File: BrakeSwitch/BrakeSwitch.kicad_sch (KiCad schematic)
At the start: 9 parts, among them J1 12V_in, J2 LightPlug, J3 5V_out, J4 Sensor_in, Q1 NMOS, U2 LMV321

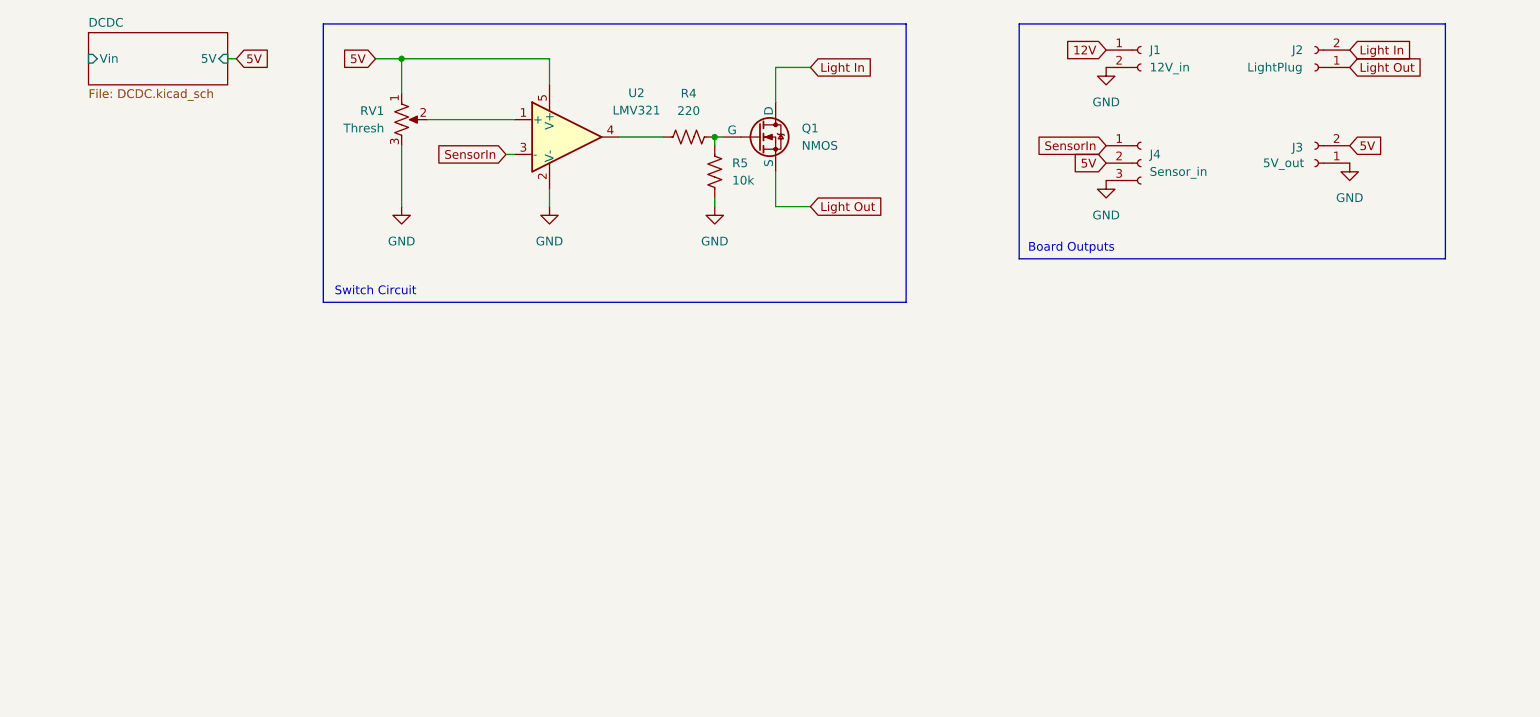
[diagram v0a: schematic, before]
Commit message: Assigned most footprints
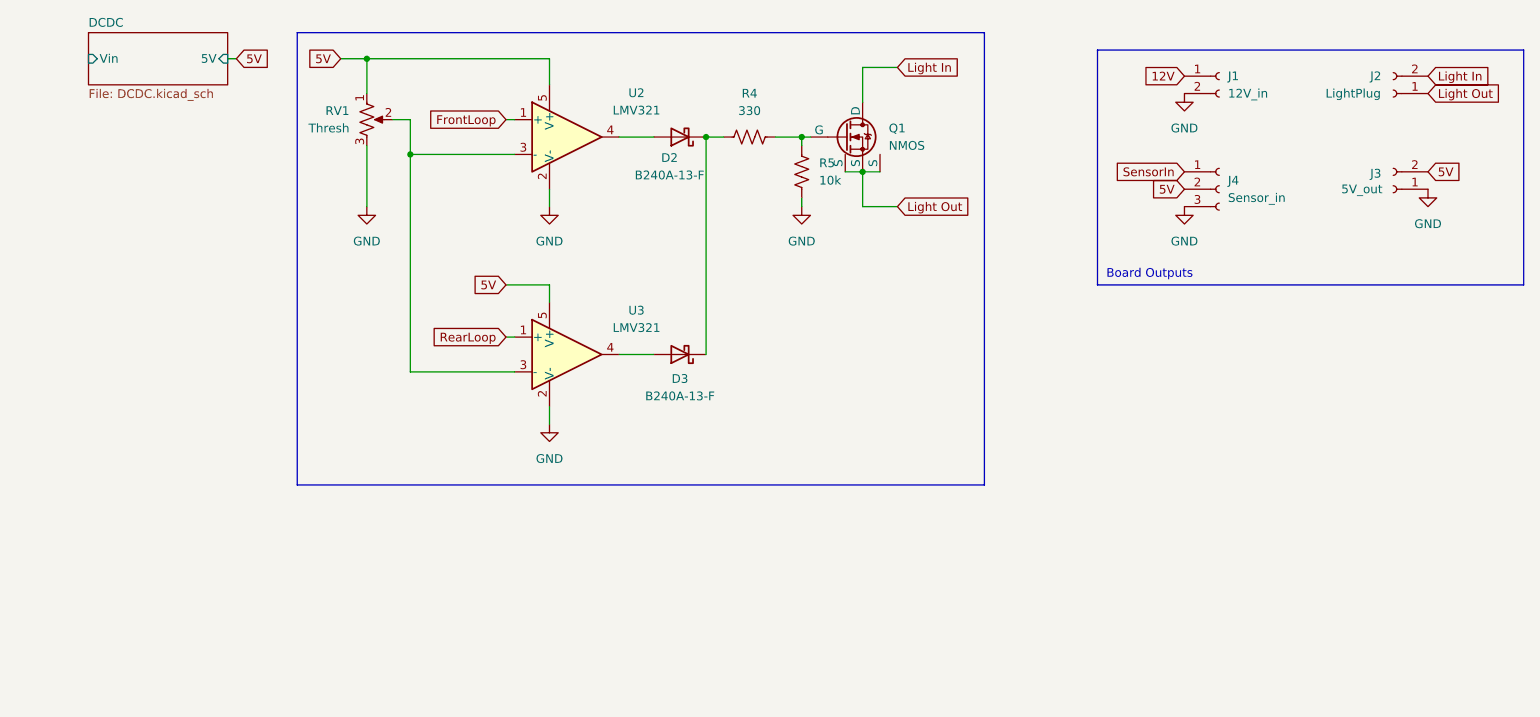
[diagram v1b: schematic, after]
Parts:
- added D2, D3: B240A-13-F, Diode_SMD:D_SMA, symbol Device:D_Schottky
- added U3: LMV321, Package_TO_SOT_SMD:SOT-23-5, symbol Amplifier_Operational:LMV321
- Q1: footprint (none) -> Package_SO:Vishay_PowerPAK_1212-8_Single; DigiKey (none) -> https://www.digikey.com/en/products/detail/onsemi/NTTFS5C45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
- R4: value 220 -> 330; footprint (none) -> Resistor_SMD:R_0603_1608Metric
- R5: footprint (none) -> Resistor_SMD:R_0603_1608Metric
- RV1: footprint (none) -> Potentiometer_THT:Potentiometer_Runtron_RM-065_Vertical; DigiKey (none) -> https://www.digikey.com/en/products/detail/amphenol-piher-s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
- U2: footprint (none) -> Package_TO_SOT_SMD:SOT-23-5; DigiKey (none) -> https://www.digikey.com/en/products/detail/texas-instrument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
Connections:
- net 5V: now also U3.5 (V+)
- net GND: now also U3.2 (V-)
- net Light In: now also Q1.5 (D); no longer Q1.1 (D)
- net Light Out: now also Q1.1 (S), Q1.2 (S)
- net SensorIn: no longer U2.3 (-)
- net at R4.1: now also D2.1 (K), D3.1 (K); no longer U2.4
- net at R4.2, R5.1: now also Q1.4 (G); no longer Q1.2 (G)
- net at RV1.2: now also U2.3 (-), U3.3 (-); no longer U2.1 (+)
- new net: D3.2 (A), U3.4
- new net: D2.2 (A), U2.4
- new net FrontLoop: U2.1 (+)
- new net RearLoop: U3.1 (+)
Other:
- note removed: "Switch Circuit"
- moved on the sheet: J1, J2, J3, J4, R4, R5, RV1

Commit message: betime
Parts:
- added J5: Back_Pads, symbol Connector:Conn_01x03_Socket
- J4: value Sensor_in -> Front_Pads
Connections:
- net SensorIn is gone; now on net FrontLoop: J4.1 (Pin_1)
- net 5V: now also J5.2 (Pin_2)
- net GND: now also J5.3 (Pin_3)
- new net BackLoop: J5.1 (Pin_1)
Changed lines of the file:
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@@
 	(rectangle
 		(start 171.45 22.86)
-		(end 233.68 57.15)
+		(end 233.68 76.2)
 		(stroke
 			(width 0)
@@
 	(text "Board Outputs"
 		(exclude_from_sim no)
-		(at 179.07 55.626 0)
+		(at 178.562 74.676 0)
 		(effects
 			(font
@@
 		)
 	)
+	(global_label "BackLoop"
+		(shape input)
+		(at 184.15 55.88 180)
+		(fields_autoplaced yes)
+		(effects
+			(font
+				(size 1.27 1.27)
+			)
+			(justify right)
+		)
+		(property "Intersheetrefs" "${INTERSHEET_REFS}"
+			(at 172.154 55.88 0)
+			(effects
+				(font
+					(size 1.27 1.27)
+				)
+				(justify right)
+				(hide yes)
+			)
+		)
+	)
 	(global_label "FrontLoop"
 		(shape input)
@@
 		)
 	)
+	(global_label "FrontLoop"
+		(shape input)
+		(at 184.15 40.64 180)
+		(fields_autoplaced yes)
+		(effects
+			(font
+				(size 1.27 1.27)
+			)
+			(justify right)
+		)
+		(property "Intersheetrefs" "${INTERSHEET_REFS}"
+			(at 171.7912 40.64 0)
+			(effects
+				(font
+					(size 1.27 1.27)
+				)
+				(justify right)
+				(hide yes)
+			)
+		)
+	)
 	(global_label "Light In"
 		(shape input)
@@
 		)
 	)
-	(global_label "SensorIn"
+	(global_label "5V"
 		(shape input)
-		(at 184.15 40.64 180)
+		(at 184.15 58.42 180)
 		(fields_autoplaced yes)
 		(effects
@@
 		)
 		(property "Intersheetrefs" "${INTERSHEET_REFS}"
-			(at 173.0006 40.64 0)
+			(at 178.8667 58.42 0)
 			(effects
 				(font
@@
 	)
 	(symbol
+		(lib_id "Connector:Conn_01x03_Socket")
+		(at 189.23 58.42 0)
+		(unit 1)
+		(exclude_from_sim no)
+		(in_bom yes)
+		(on_board yes)
+		(dnp no)
+		(fields_autoplaced yes)
+		(property "Reference" "J5"
+			(at 190.5 57.1499 0)
+			(effects
+				(font
+					(size 1.27 1.27)
+				)
+				(justify left)
+			)
+		)
+		(property "Value" "Back_Pads"
+			(at 190.5 59.6899 0)
+			(effects
+				(font
+					(size 1.27 1.27)
+				)
+				(justify left)
+			)
+		)
+		(property "Footprint" ""
+			(at 189.23 58.42 0)
+			(effects
+				(font
+					(size 1.27 1.27)
+				)
+				(hide yes)
+			)
+		)
+		(property "Datasheet" "~"
+			(at 189.23 58.42 0)
+			(effects
+				(font
+					(size 1.27 1.27)
+				)
+				(hide yes)
+			)
+		)
+		(property "Description" "Generic connector, single row, 01x03, script generated"
+			(at 189.23 58.42 0)
+			(effects
+				(font
+					(size 1.27 1.27)
+				)
+				(hide yes)
+			)
+		)
+		(pin "2"
+		)
+		(pin "1"
+		)
+		(pin "3"
+		)
+		(instances
+			(project "BrakeSwitch"
+				(path "/fe3f2fb8-8742-4f31-813f-1dad9d418d71"
+					(reference "J5")
+					(unit 1)
+				)
+			)
+		)
+	)
+	(symbol
 		(lib_id "Connector:Conn_01x02_Socket")
 		(at 214.63 43.18 180)
@@
 	)
 	(symbol
+		(lib_id "power:GND")
+		(at 184.15 60.96 0)
+		(unit 1)
+		(exclude_from_sim no)
+		(in_bom yes)
+		(on_board yes)
+		(dnp no)
+		(fields_autoplaced yes)
+		(property "Reference" "#PWR013"
+			(at 184.15 67.31 0)
+			(effects
+				(font
+					(size 1.27 1.27)
+				)
+				(hide yes)
+			)
+		)
+		(property "Value" "GND"
+			(at 184.15 66.04 0)
+			(effects
+				(font
+					(size 1.27 1.27)
+				)
+			)
+		)
+		(property "Footprint" ""
+			(at 184.15 60.96 0)
+			(effects
+				(font
+					(size 1.27 1.27)
+				)
+				(hide yes)
+			)
+		)
+		(property "Datasheet" ""
+			(at 184.15 60.96 0)
+			(effects
+				(font
+					(size 1.27 1.27)
+				)
+				(hide yes)
+			)
+		)
+		(property "Description" "Power symbol creates a global label with name \"GND\" , ground"
+			(at 184.15 60.96 0)
+			(effects
+				(font
+					(size 1.27 1.27)
+				)
+				(hide yes)
+			)
+		)
+		(pin "1"
+		)
+		(instances
+			(project "BrakeSwitch"
+				(path "/fe3f2fb8-8742-4f31-813f-1dad9d418d71"
+					(reference "#PWR013")
+					(unit 1)
+				)
+			)
+		)
+	)
+	(symbol
 		(lib_id "Connector:Conn_01x03_Socket")
 		(at 189.23 43.18 0)
@@
 			)
 		)
-		(property "Value" "Sensor_in"
+		(property "Value" "Front_Pads"
 			(at 190.5 44.4499 0)
 			(effects

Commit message: Basic layout done
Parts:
- added J6: 12V_in, AA-Custom:SolderPad_01x02, symbol Connector:Conn_01x02_Socket
- J1, J2, J3: footprint (none) -> AA-Custom:SolderPad_01x02
- J4, J5: footprint (none) -> AA-Custom:SolderPad_01x03
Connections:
- net BackLoop is gone; now on net RearLoop: J5.1 (Pin_1)
- net GND: now also J6.2 (Pin_2)
- new net 12V_out: J6.1 (Pin_1)
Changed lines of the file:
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@@
 		)
 	)
-	(global_label "BackLoop"
+	(global_label "RearLoop"
 		(shape input)
 		(at 184.15 55.88 180)
@@
 		)
 		(property "Intersheetrefs" "${INTERSHEET_REFS}"
-			(at 172.154 55.88 0)
+			(at 172.3959 55.88 0)
 			(effects
 				(font
@@
 		)
 	)
+	(global_label "12V_out"
+		(shape input)
+		(at 219.71 55.88 0)
+		(fields_autoplaced yes)
+		(effects
+			(font
+				(size 1.27 1.27)
+			)
+			(justify left)
+		)
+		(property "Intersheetrefs" "${INTERSHEET_REFS}"
+			(at 230.1941 55.88 0)
+			(effects
+				(font
+					(size 1.27 1.27)
+				)
+				(justify left)
+				(hide yes)
+			)
+		)
+	)
 	(global_label "5V"
 		(shape input)
@@
 	)
 	(symbol
+		(lib_id "Connector:Conn_01x02_Socket")
+		(at 214.63 55.88 0)
+		(mirror y)
+		(unit 1)
+		(exclude_from_sim no)
+		(in_bom yes)
+		(on_board yes)
+		(dnp no)
+		(fields_autoplaced yes)
+		(property "Reference" "J6"
+			(at 213.36 55.8799 0)
+			(effects
+				(font
+					(size 1.27 1.27)
+				)
+				(justify left)
+			)
+		)
+		(property "Value" "12V_in"
+			(at 213.36 58.4199 0)
+			(effects
+				(font
+					(size 1.27 1.27)
+				)
+				(justify left)
+			)
+		)
+		(property "Footprint" "AA-Custom:SolderPad_01x02"
+			(at 214.63 55.88 0)
+			(effects
+				(font
+					(size 1.27 1.27)
+				)
+				(hide yes)
+			)
+		)
+		(property "Datasheet" "~"
+			(at 214.63 55.88 0)
+			(effects
+				(font
+					(size 1.27 1.27)
+				)
+				(hide yes)
+			)
+		)
+		(property "Description" "Generic connector, single row, 01x02, script generated"
+			(at 214.63 55.88 0)
+			(effects
+				(font
+					(size 1.27 1.27)
+				)
+				(hide yes)
+			)
+		)
+		(pin "2"
+		)
+		(pin "1"
+		)
+		(instances
+			(project "BrakeSwitch"
+				(path "/fe3f2fb8-8742-4f31-813f-1dad9d418d71"
+					(reference "J6")
+					(unit 1)
+				)
+			)
+		)
+	)
+	(symbol
 		(lib_id "Device:R_US")
 		(at 120.65 35.56 90)
@@
 	(symbol
 		(lib_id "power:GND")
+		(at 219.71 58.42 0)
+		(mirror y)
+		(unit 1)
+		(exclude_from_sim no)
+		(in_bom yes)
+		(on_board yes)
+		(dnp no)
+		(fields_autoplaced yes)
+		(property "Reference" "#PWR016"
+			(at 219.71 64.77 0)
+			(effects
+				(font
+					(size 1.27 1.27)
+				)
+				(hide yes)
+			)
+		)
+		(property "Value" "GND"
+			(at 219.71 63.5 0)
+			(effects
+				(font
+					(size 1.27 1.27)
+				)
+			)
+		)
+		(property "Footprint" ""
+			(at 219.71 58.42 0)
+			(effects
+				(font
+					(size 1.27 1.27)
+				)
+				(hide yes)
+			)
+		)
+		(property "Datasheet" ""
+			(at 219.71 58.42 0)
+			(effects
+				(font
+					(size 1.27 1.27)
+				)
+				(hide yes)
+			)
+		)
+		(property "Description" "Power symbol creates a global label with name \"GND\" , ground"
+			(at 219.71 58.42 0)
+			(effects
+				(font
+					(size 1.27 1.27)
+				)
+				(hide yes)
+			)
+		)
+		(pin "1"
+		)
+		(instances
+			(project "BrakeSwitch"
+				(path "/fe3f2fb8-8742-4f31-813f-1dad9d418d71"
+					(reference "#PWR016")
+					(unit 1)
+				)
+			)
+		)
+	)
+	(symbol
+		(lib_id "power:GND")
 		(at 64.77 45.72 0)
 		(unit 1)
@@
 			)
 		)
-		(property "Footprint" ""
+		(property "Footprint" "AA-Custom:SolderPad_01x02"
 			(at 189.23 26.67 0)
 			(effects
@@
 			)
 		)
-		(property "Footprint" ""
+		(property "Footprint" "AA-Custom:SolderPad_01x02"
 			(at 214.63 29.21 0)
 			(effects
@@
 			)
 		)
-		(property "Footprint" ""
+		(property "Footprint" "AA-Custom:SolderPad_01x03"
 			(at 189.23 58.42 0)
 			(effects
@@
 			)
 		)
-		(property "Footprint" ""
+		(property "Footprint" "AA-Custom:SolderPad_01x02"
 			(at 214.63 43.18 0)
 			(effects
@@
 			)
 		)
-		(property "Footprint" ""
+		(property "Footprint" "AA-Custom:SolderPad_01x03"
 			(at 189.23 43.18 0)
 			(effects
@@
 					(reference "Q1")
 					(unit 1)
+				)
+				(path "/fe3f2fb8-8742-4f31-813f-1dad9d418d71/293b1cf4-e9c5-4398-be38-45432f0835da"
+					(reference "Q1")
+					(unit 1)

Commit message: Some feedback and layout
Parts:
- added H1: MountingHole, MountingHole:MountingHole_6.5mm_Pad, symbol Mechanical:MountingHole
- added RV2: Thresh, Potentiometer_THT:Potentiometer_Runtron_RM-065_Vertical, symbol Device:R_Potentiometer_US
- J4: value Front_Pads -> Front_Loop
- J5: value Back_Pads -> Rear_Loop
- J6: value 12V_in -> 12V_Out
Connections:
- net 5V: now also RV2.1
- net GND: now also RV2.3
- net at RV1.2, U2.3 (-): no longer U3.3 (-)
- new net: RV2.2, U3.3 (-)
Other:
- note added: "Board ports"
- note removed: "Board Outputs"
- moved on the sheet: RV1

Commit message: Progress save
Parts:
- removed J2: LightPlug, AA-Custom:SolderPad_01x02, symbol Connector:Conn_01x02_Socket
- added J2: Signal_Breakout, AA-Custom:SolderPad_01x04, symbol Connector:Conn_01x04_Socket
- added J7: Front_Brake_Switch, AA-Custom:SolderPad_01x02, symbol Connector:Conn_01x02_Socket
- added J8: Rear_Brake_Switch, AA-Custom:SolderPad_01x02, symbol Connector:Conn_01x02_Socket
- added J9: Light_In, AA-Custom:SolderPad_01x01, symbol Connector:Conn_01x01_Socket
- added SW1: AT SW-R2-2B-F-1-0, AA-Custom:SPDT_PanelMount_Switch, symbol Switch:SW_Nidec_CAS-120A1
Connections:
- net Light Out is gone; now on net GND: Q1.1 (S), Q1.2 (S), Q1.3 (S)
- net 5V: now also J2.2 (Pin_2)
- net FrontLoop: now also J2.4 (Pin_4)
- net GND: now also J2.1 (Pin_1), J7.1 (Pin_1), J8.2 (Pin_2)
- net Light In: now also J9.1 (Pin_1), SW1.2 (B); no longer Q1.5 (D)
- net RearLoop: now also J2.3 (Pin_3)
- new net: Q1.5 (D), SW1.1 (C)
- new net SwitchF+: J7.2 (Pin_2), J8.1 (Pin_1), SW1.3 (A)
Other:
- moved on the sheet: D2, D3, H1, J1, J3, J4, J5, J6, Q1, R4, R5, RV1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

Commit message: Layout doneish
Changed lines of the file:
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@@
+	)
+	(junction
+		(at 147.32 53.34)
+		(diameter 0)
+		(color 0 0 0 0)
+	)
+	(junction
+		(at 127 48.26)
+		(diameter 0)
+		(color 0 0 0 0)
 	)
 	(junction
@@
 		(color 0 0 0 0)
 	)
-	(junction
-		(at 127 48.26)
-		(diameter 0)
-		(color 0 0 0 0)
-	)
 	(wire
 		(pts
@@
 	(wire
 		(pts
+			(xy 147.32 53.34) (xy 148.59 53.34)
+		)
+		(stroke
+			(width 0)
+			(type default)
+		)
+	)
+	(wire
+		(pts
 			(xy 147.32 55.88) (xy 148.59 55.88)
 		)
@@
 	(wire
 		(pts
+			(xy 147.32 53.34) (xy 147.32 50.8)
+		)
+		(stroke
+			(width 0)
+			(type default)
+		)
+	)
+	(wire
+		(pts
 			(xy 90.17 36.83) (xy 90.17 40.64)
 		)
@@
 	(wire
 		(pts
+			(xy 147.32 55.88) (xy 147.32 58.42)
+		)
+		(stroke
+			(width 0)
+			(type default)
+		)
+	)
+	(wire
+		(pts
 			(xy 83.82 45.72) (xy 85.09 45.72)
 		)
@@
 	(wire
 		(pts
-			(xy 147.32 53.34) (xy 148.59 53.34)
+			(xy 147.32 50.8) (xy 148.59 50.8)
 		)
 		(stroke
@@
 	(wire
 		(pts
-			(xy 147.32 58.42) (xy 147.32 55.88)
-		)
-		(stroke
-			(width 0)
-			(type default)
-		)
-	)
-	(wire
-		(pts
 			(xy 148.59 46.99) (xy 147.32 46.99)
 		)
@@
 	(wire
 		(pts
-			(xy 147.32 55.88) (xy 147.32 53.34)
+			(xy 147.32 53.34) (xy 147.32 55.88)
 		)
 		(stroke
@@
 		)
 	)
+	(global_label "GND"
+		(shape input)
+		(at 148.59 55.88 0)
+		(fields_autoplaced yes)
+		(effects
+			(font
+				(size 1.27 1.27)
+			)
+			(justify left)
+		)
+		(property "Intersheetrefs" "${INTERSHEET_REFS}"
+			(at 155.4457 55.88 0)
+			(effects
+				(font
+					(size 1.27 1.27)
+				)
+				(justify left)
+				(hide yes)
+			)
+		)
+	)
 	(global_label "5V"
 		(shape input)
@@
 	(global_label "SwitchR-"
 		(shape input)
-		(at 148.59 55.88 0)
-		(fields_autoplaced yes)
-		(effects
-			(font
-				(size 1.27 1.27)
-			)
-			(justify left)
-		)
-		(property "Intersheetrefs" "${INTERSHEET_REFS}"
-			(at 160.5257 55.88 0)
+		(at 148.59 53.34 0)
+		(fields_autoplaced yes)
+		(effects
+			(font
+				(size 1.27 1.27)
+			)
+			(justify left)
+		)
+		(property "Intersheetrefs" "${INTERSHEET_REFS}"
+			(at 160.5257 53.34 0)
 			(effects
 				(font
@@
 	(global_label "SwitchF-"
 		(shape input)
-		(at 148.59 53.34 0)
-		(fields_autoplaced yes)
-		(effects
-			(font
-				(size 1.27 1.27)
-			)
-			(justify left)
-		)
-		(property "Intersheetrefs" "${INTERSHEET_REFS}"
-			(at 160.3443 53.34 0)
-			(effects
-				(font
+		(at 148.59 50.8 0)
+		(fields_autoplaced yes)
+		(effects
+			(font
+				(size 1.27 1.27)
+			)
+			(justify left)
+		)
+		(property "Intersheetrefs" "${INTERSHEET_REFS}"
+			(at 160.3443 50.8 0)
+			(effects
+				(font

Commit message: Starting traces
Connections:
- net 12V_out is gone; now on net 12V: J6.1 (Pin_1)
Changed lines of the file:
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@@
 		)
 	)
-	(global_label "12V_out"
+	(global_label "12V"
 		(shape input)
 		(at 219.71 58.42 0)
@@
 		)
 		(property "Intersheetrefs" "${INTERSHEET_REFS}"
-			(at 230.1941 58.42 0)
+			(at 226.2028 58.42 0)
 			(effects
 				(font
